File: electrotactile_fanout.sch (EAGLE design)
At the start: 3 parts, among them J1 2X17_PTH_RA-FEMALE, J2 1X33_MOLEX_FPC_FPC_RIBBON-CAB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

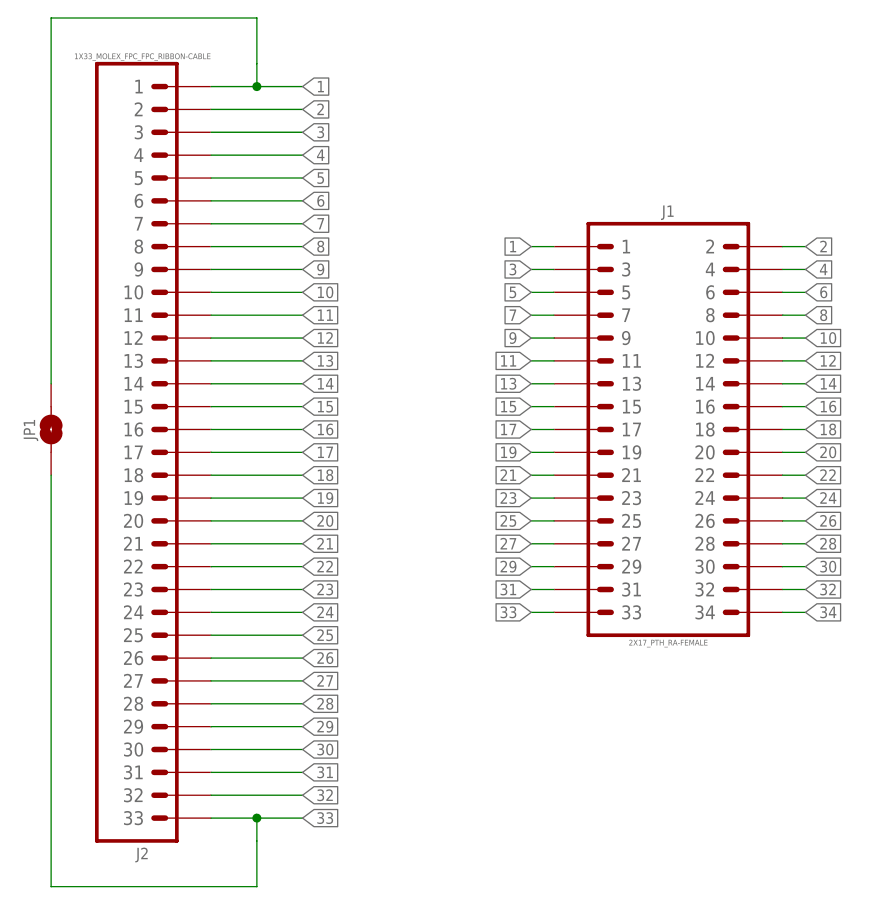
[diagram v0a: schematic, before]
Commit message: Update libraries with metadata.
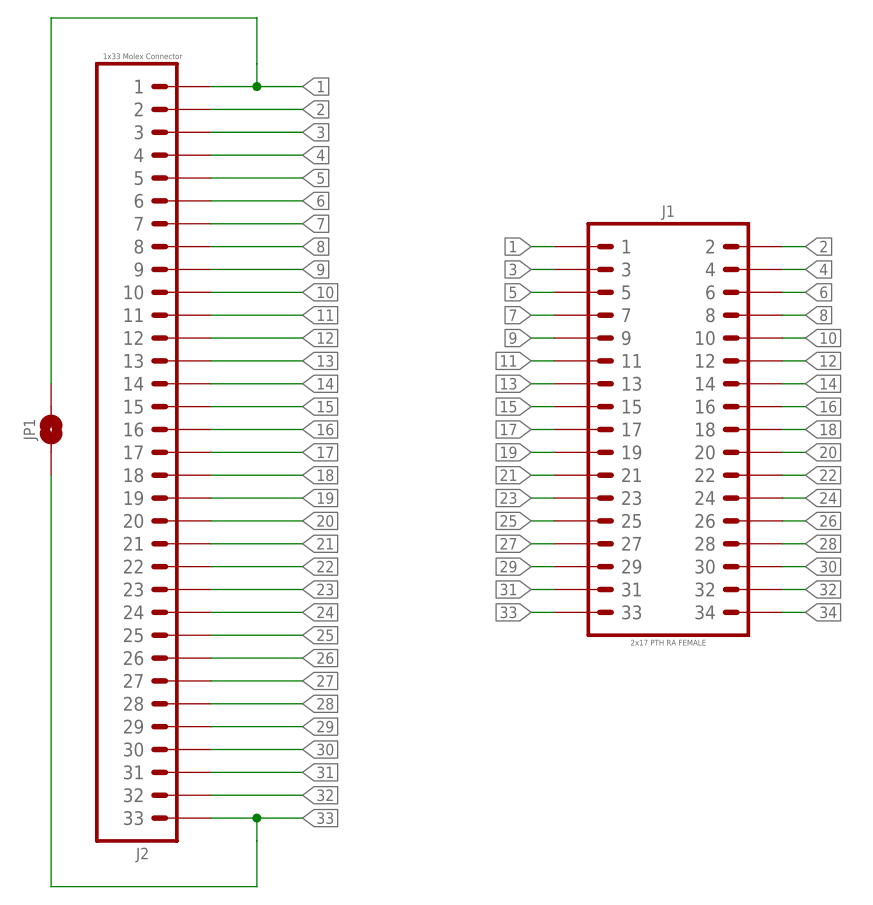
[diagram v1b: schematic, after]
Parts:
- J1: value 2X17_PTH_RA-FEMALE -> 2x17 PTH RA FEMALE
- J2: value 1X33_MOLEX_FPC_FPC_RIBBON-CABLE -> 1x33 Molex Connector
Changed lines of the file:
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@@
 <parts>
 <part name="JP1" library="PiB_connectors" deviceset="JUMPER_SMD_2-PAD_NO" device="_SILK"/>
-<part name="J2" library="PiB_connectors" deviceset="1X33_MOLEX_FPC" device="_FPC_RIBBON-CABLE" package3d_urn="urn:adsk.eagle:package:3945547/2"/>
-<part name="J1" library="PiB_connectors" deviceset="2X17" device="_PTH_RA-FEMALE" package3d_urn="urn:adsk.eagle:package:3955995/2"/>
+<part name="J2" library="PiB_connectors" deviceset="1X33_MOLEX_FPC" device="_FPC_RIBBON-CABLE" package3d_urn="urn:adsk.eagle:package:3945547/2" value="1x33 Molex Connector"/>
+<part name="J1" library="PiB_connectors" deviceset="2X17" device="_PTH_RA-FEMALE" package3d_urn="urn:adsk.eagle:package:3955995/2" value="2x17 PTH RA FEMALE"/>
 </parts>
 <sheets>
